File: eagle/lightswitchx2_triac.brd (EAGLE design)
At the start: 61.5 x 62 mm, 29 parts, among them Q1 KA78R33CTU, T1 BT136, T2 BT136, U1 PCA9536D, U2 ESP01

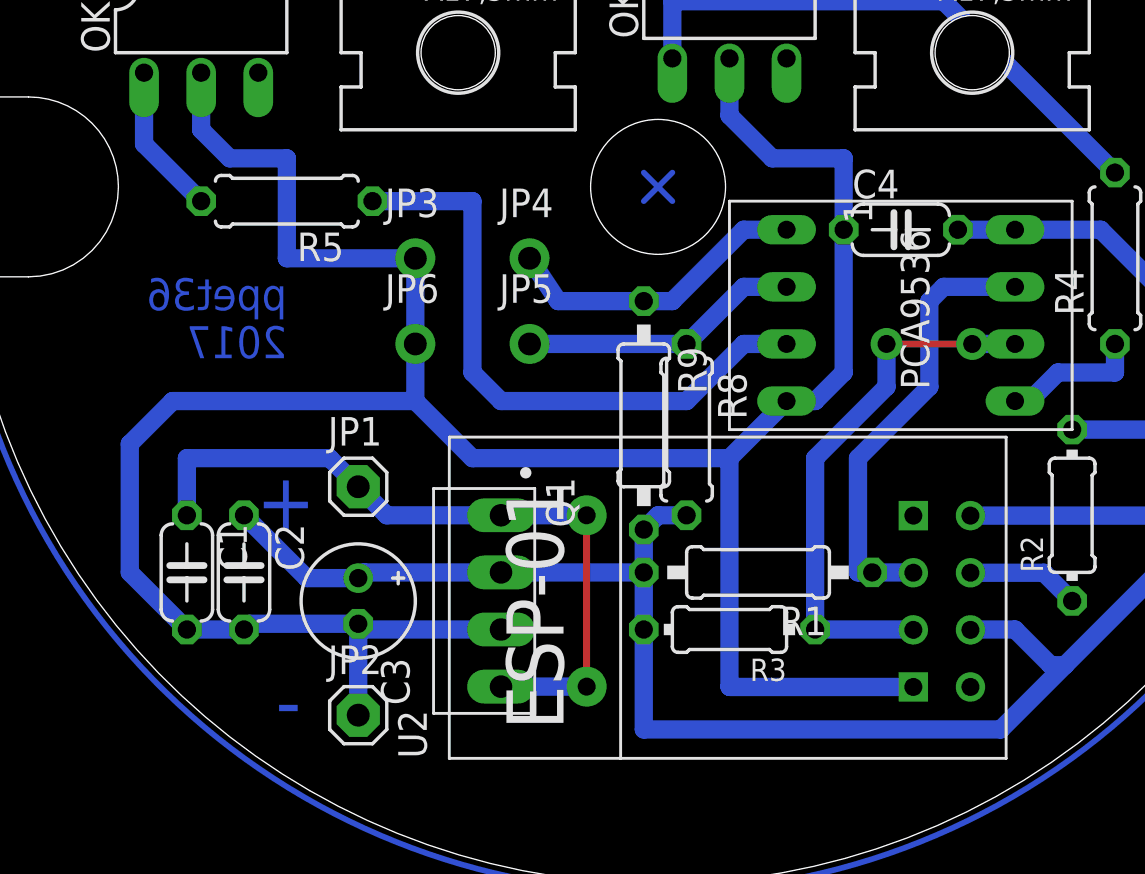
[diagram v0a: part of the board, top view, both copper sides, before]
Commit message: Added some 100n capacitors
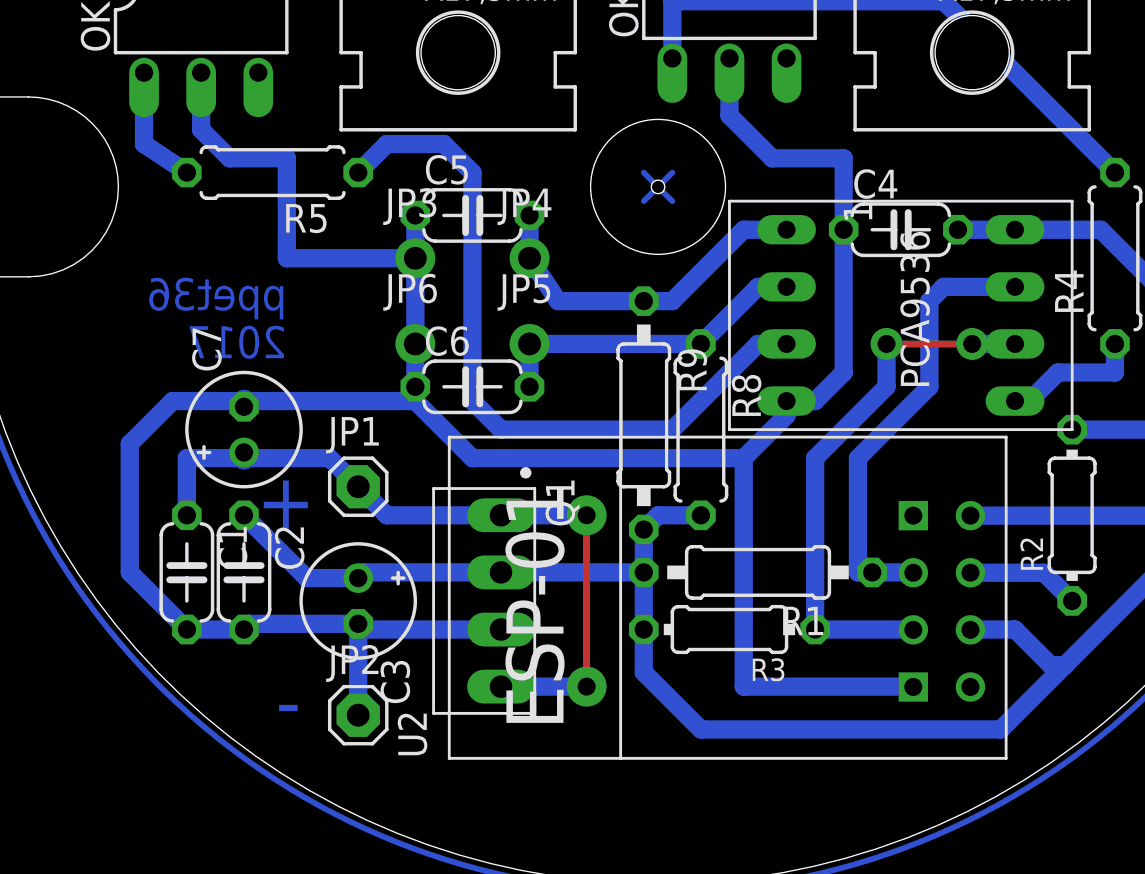
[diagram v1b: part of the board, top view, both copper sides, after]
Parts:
- added C5, C6: 100n, rcl:C050-024X044
- added C7: 330u, rcl:E2-5
- R8, R9: value 10K -> 4K7
- moved R5 1.42 mm to (15.9, 31.8)
- moved R8 0.63 mm to (34.9, 20.3)
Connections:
- net N$1: now also C7.+
- net N$11: now also C5.2
- net N$14: now also C6.2
- net VSS: now also C5.1, C6.1, C7.-
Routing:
- net N$9: track 27.6 -> 32.4 mm
- net N$11: track 13.8 -> 15.7 mm
- net N$14: track 12.5 -> 14.4 mm
- net VSS: track 122.4 -> 124.3 mm
- net N$5: track 6.77 -> 5.46 mm
- net VDD: track 97.3 -> 96.5 mm
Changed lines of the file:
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@@
 <circle x="33.02" y="31.115" radius="31.3731125" width="0.254" layer="16"/>
 <dimension x1="33.02" y1="-0.2581125" x2="33.02" y2="62.4881125" x3="-2.54" y3="31.115" textsize="1.778" layer="20" dtype="diameter"/>
+<hole x="33.02" y="31.115" drill="0.6"/>
 </plain>
 <attributes>
@@
 <element name="JP4" library="adafruit" package="1X01-CLEANBIG" value="SW1" x="27.305" y="27.94"/>
 <element name="JP5" library="adafruit" package="1X01-CLEANBIG" value="SW2" x="27.305" y="24.13"/>
-<element name="R8" library="rcl" package="0207/7" value="10K" x="34.29" y="20.32" rot="R270"/>
-<element name="R9" library="rcl" package="0207/10" value="10K" x="32.385" y="20.955" rot="R270"/>
+<element name="R8" library="rcl" package="0207/7" value="4K7" x="34.925" y="20.32" rot="R270"/>
+<element name="R9" library="rcl" package="0207/10" value="4K7" x="32.385" y="20.955" rot="R270"/>
 <element name="JP6" library="adafruit" package="1X01-CLEANBIG" value="SW_GND" x="22.225" y="24.13"/>
 <element name="R1" library="rcl" package="0207/10" value="10K" x="37.465" y="13.97" rot="R180"/>
@@
 <element name="T2" library="triac" package="TO220AB" value="BT136" x="46.99" y="48.26" rot="R180"/>
 <element name="R4" library="rcl" package="0207/7" value="220" x="53.34" y="27.94" rot="R90"/>
-<element name="R5" library="rcl" package="0207/7" value="220" x="16.51" y="30.48" rot="R180"/>
+<element name="R5" library="rcl" package="0207/7" value="220" x="15.875" y="31.75" rot="R180"/>
 <element name="R6" library="rcl" package="0207/7" value="330" x="33.655" y="49.53" rot="R90"/>
 <element name="R7" library="rcl" package="0207/7" value="330" x="30.48" y="49.53" rot="R90"/>
@@
 <element name="U$3" library="LEG-1A-5" package="PAD" value="PAD" x="29.845" y="58.42"/>
 <element name="C4" library="rcl" package="C050-024X044" value="100n" x="43.815" y="29.21"/>
+<element name="C5" library="rcl" package="C050-024X044" value="100n" x="24.765" y="29.845"/>
+<element name="C6" library="rcl" package="C050-024X044" value="100n" x="24.765" y="22.225"/>
+<element name="C7" library="rcl" package="E2-5" value="330u" x="14.605" y="20.32" rot="R90"/>
 </elements>
 <signals>
@@
 <wire x1="20.955" y1="16.51" x2="26.035" y2="16.51" width="0.8128" layer="16"/>
 <wire x1="12.065" y1="16.51" x2="12.065" y2="19.05" width="0.8128" layer="16"/>
-<wire x1="12.065" y1="19.05" x2="18.415" y2="19.05" width="0.8128" layer="16"/>
+<wire x1="12.065" y1="19.05" x2="14.605" y2="19.05" width="0.8128" layer="16"/>
+<wire x1="14.605" y1="19.05" x2="18.415" y2="19.05" width="0.8128" layer="16"/>
 <wire x1="18.415" y1="19.05" x2="19.685" y2="17.78" width="0.8128" layer="16"/>
+<contactref element="C7" pad="+"/>
+<wire x1="14.605" y1="19.304" x2="14.605" y2="19.05" width="1.016" layer="16"/>
 </signal>
 <signal name="VSS">
@@
 <wire x1="14.605" y1="11.43" x2="12.065" y2="11.43" width="0.8128" layer="16"/>
 <wire x1="22.225" y1="27.94" x2="22.225" y2="24.13" width="0.8128" layer="16"/>
-<wire x1="22.225" y1="24.13" x2="22.225" y2="21.59" width="0.8128" layer="16"/>
-<wire x1="24.765" y1="19.05" x2="36.195" y2="19.05" width="0.8128" layer="16"/>
+<wire x1="22.225" y1="24.13" x2="22.225" y2="22.225" width="0.8128" layer="16"/>
+<wire x1="22.225" y1="22.225" x2="22.225" y2="21.59" width="0.8128" layer="16"/>
+<wire x1="24.765" y1="19.05" x2="36.83" y2="19.05" width="0.8128" layer="16"/>
 <wire x1="24.765" y1="19.05" x2="22.225" y2="21.59" width="0.8128" layer="16"/>
-<wire x1="44.3725" y1="8.875" x2="36.21" y2="8.875" width="0.8128" layer="16"/>
-<wire x1="36.21" y1="8.875" x2="36.195" y2="8.89" width="0.8128" layer="16"/>
-<wire x1="36.195" y1="8.89" x2="36.195" y2="19.05" width="0.8128" layer="16"/>
-<wire x1="38.735" y1="21.59" x2="36.195" y2="19.05" width="0.8128" layer="16"/>
+<wire x1="36.83" y1="8.89" x2="36.83" y2="19.05" width="0.8128" layer="16"/>
 <wire x1="12.065" y1="11.43" x2="9.525" y2="13.97" width="0.8128" layer="16"/>
 <wire x1="9.525" y1="13.97" x2="9.525" y2="19.685" width="0.8128" layer="16"/>
 <wire x1="9.525" y1="19.685" x2="11.43" y2="21.59" width="0.8128" layer="16"/>
-<wire x1="11.43" y1="21.59" x2="22.225" y2="21.59" width="0.8128" layer="16"/>
+<wire x1="11.43" y1="21.59" x2="14.605" y2="21.59" width="0.8128" layer="16"/>
 <contactref element="JP6" pad="1"/>
 <contactref element="OK2" pad="2"/>
+<wire x1="14.605" y1="21.59" x2="22.225" y2="21.59" width="0.8128" layer="16"/>
 <wire x1="41.275" y1="29.21" x2="41.275" y2="22.86" width="0.8128" layer="16"/>
 <wire x1="41.275" y1="22.86" x2="40.005" y2="21.59" width="0.8128" layer="16"/>
@@
 <wire x1="38.1" y1="32.385" x2="41.275" y2="32.385" width="0.8128" layer="16"/>
 <wire x1="41.275" y1="32.385" x2="41.275" y2="29.21" width="0.8128" layer="16"/>
+<contactref element="C5" pad="1"/>
+<contactref element="C6" pad="1"/>
+<wire x1="22.225" y1="29.845" x2="22.225" y2="27.94" width="0.8128" layer="16"/>
+<contactref element="C7" pad="-"/>
+<wire x1="14.605" y1="21.336" x2="14.605" y2="21.59" width="1.016" layer="16"/>
+<wire x1="36.83" y1="19.05" x2="38.735" y2="20.955" width="0.8128" layer="16"/>
+<wire x1="38.735" y1="20.955" x2="38.735" y2="21.59" width="0.8128" layer="16"/>
+<wire x1="44.3725" y1="8.875" x2="44.3575" y2="8.89" width="0.8128" layer="16"/>
+<wire x1="44.3575" y1="8.89" x2="36.83" y2="8.89" width="0.8128" layer="16"/>
 </signal>
 <signal name="N$7">
@@
 <signal name="N$9">
 <contactref element="U1" pad="P$3"/>
-<wire x1="38.735" y1="24.13" x2="36.83" y2="24.13" width="0.8128" layer="16"/>
-<wire x1="36.83" y1="24.13" x2="34.29" y2="21.59" width="0.8128" layer="16"/>
-<wire x1="34.29" y1="21.59" x2="26.035" y2="21.59" width="0.8128" layer="16"/>
-<wire x1="26.035" y1="21.59" x2="24.765" y2="22.86" width="0.8128" layer="16"/>
 <contactref element="R5" pad="1"/>
-<wire x1="24.765" y1="22.86" x2="24.765" y2="30.48" width="0.8128" layer="16"/>
-<wire x1="20.32" y1="30.48" x2="24.765" y2="30.48" width="0.8128" layer="16"/>
+<wire x1="24.765" y1="21.59" x2="24.765" y2="31.75" width="0.8128" layer="16"/>
+<wire x1="38.735" y1="24.13" x2="37.465" y2="24.13" width="0.8128" layer="16"/>
+<wire x1="37.465" y1="24.13" x2="33.655" y2="20.32" width="0.8128" layer="16"/>
+<wire x1="33.655" y1="20.32" x2="26.035" y2="20.32" width="0.8128" layer="16"/>
+<wire x1="26.035" y1="20.32" x2="24.765" y2="21.59" width="0.8128" layer="16"/>
+<wire x1="24.765" y1="31.75" x2="23.495" y2="33.02" width="0.8128" layer="16"/>
+<wire x1="23.495" y1="33.02" x2="20.955" y2="33.02" width="0.8128" layer="16"/>
+<wire x1="20.955" y1="33.02" x2="19.685" y2="31.75" width="0.8128" layer="16"/>
 </signal>
 <signal name="N$2">
@@
 <wire x1="19.685" y1="13.716" x2="19.939" y2="13.97" width="0.8128" layer="16"/>
 <wire x1="19.939" y1="13.97" x2="26.035" y2="13.97" width="0.8128" layer="16"/>
-<wire x1="48.26" y1="6.985" x2="32.385" y2="6.985" width="0.8128" layer="16"/>
-<wire x1="32.385" y1="6.985" x2="32.385" y2="11.43" width="0.8128" layer="16"/>
 <wire x1="48.26" y1="6.985" x2="51.1175" y2="9.8425" width="0.8128" layer="16"/>
 <wire x1="51.1175" y1="9.8425" x2="55.88" y2="14.605" width="0.8128" layer="16"/>
@@
 <contactref element="R8" pad="2"/>
 <wire x1="32.385" y1="15.875" x2="33.02" y2="16.51" width="0.8128" layer="16"/>
-<wire x1="33.02" y1="16.51" x2="34.29" y2="16.51" width="0.8128" layer="16"/>
+<wire x1="33.02" y1="16.51" x2="34.925" y2="16.51" width="0.8128" layer="16"/>
 <contactref element="R1" pad="2"/>
 <wire x1="26.035" y1="13.97" x2="32.385" y2="13.97" width="0.8128" layer="16"/>
@@
 <wire x1="55.88" y1="26.035" x2="52.705" y2="29.21" width="0.8128" layer="16"/>
 <wire x1="52.705" y1="29.21" x2="48.895" y2="29.21" width="0.8128" layer="16"/>
+<wire x1="48.26" y1="6.985" x2="34.925" y2="6.985" width="0.8128" layer="16"/>
+<wire x1="34.925" y1="6.985" x2="32.385" y2="9.525" width="0.8128" layer="16"/>
+<wire x1="32.385" y1="9.525" x2="32.385" y2="11.43" width="0.8128" layer="16"/>
 </signal>
 <signal name="N$11">
@@
 <contactref element="R9" pad="1"/>
 <wire x1="32.385" y1="26.035" x2="33.655" y2="26.035" width="0.8128" layer="16"/>
+<contactref element="C5" pad="2"/>
+<wire x1="27.305" y1="29.845" x2="27.305" y2="27.94" width="0.8128" layer="16"/>
 </signal>
 <signal name="N$14">
 <contactref element="JP5" pad="1"/>
 <contactref element="U1" pad="P$2"/>
-<wire x1="36.83" y1="26.67" x2="38.735" y2="26.67" width="0.8128" layer="16"/>
-<wire x1="36.83" y1="26.67" x2="34.29" y2="24.13" width="0.8128" layer="16"/>
-<wire x1="34.29" y1="24.13" x2="27.305" y2="24.13" width="0.8128" layer="16"/>
+<wire x1="37.465" y1="26.67" x2="38.735" y2="26.67" width="0.8128" layer="16"/>
+<wire x1="37.465" y1="26.67" x2="34.925" y2="24.13" width="0.8128" layer="16"/>
+<wire x1="34.925" y1="24.13" x2="27.305" y2="24.13" width="0.8128" layer="16"/>
 <contactref element="R8" pad="1"/>
+<contactref element="C6" pad="2"/>
+<wire x1="27.305" y1="24.13" x2="27.305" y2="22.225" width="0.8128" layer="16"/>
 </signal>
 <signal name="N$3">
@@
 <contactref element="OK2" pad="1"/>
 <wire x1="10.16" y1="36.195" x2="10.16" y2="33.02" width="0.8128" layer="16"/>
-<wire x1="10.16" y1="33.02" x2="12.7" y2="30.48" width="0.8128" layer="16"/>
+<wire x1="10.16" y1="33.02" x2="12.065" y2="31.75" width="0.8128" layer="16"/>
 </signal>
 <signal name="N$8">
